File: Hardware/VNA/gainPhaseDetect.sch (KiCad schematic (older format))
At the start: 34 parts, among them U14 F2923, U15 AD8302

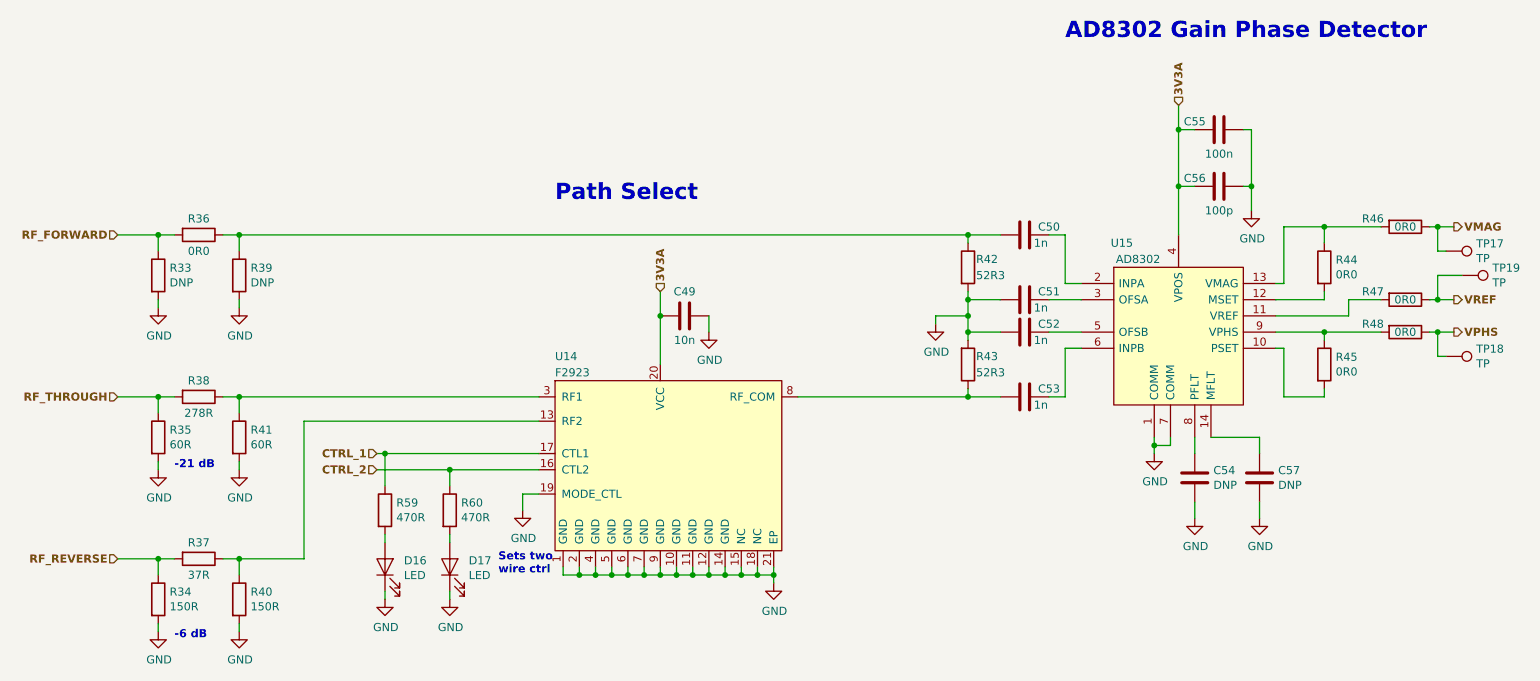
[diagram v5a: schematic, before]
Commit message: fix KiCad 5.1.0 bold after plot issue on schematics
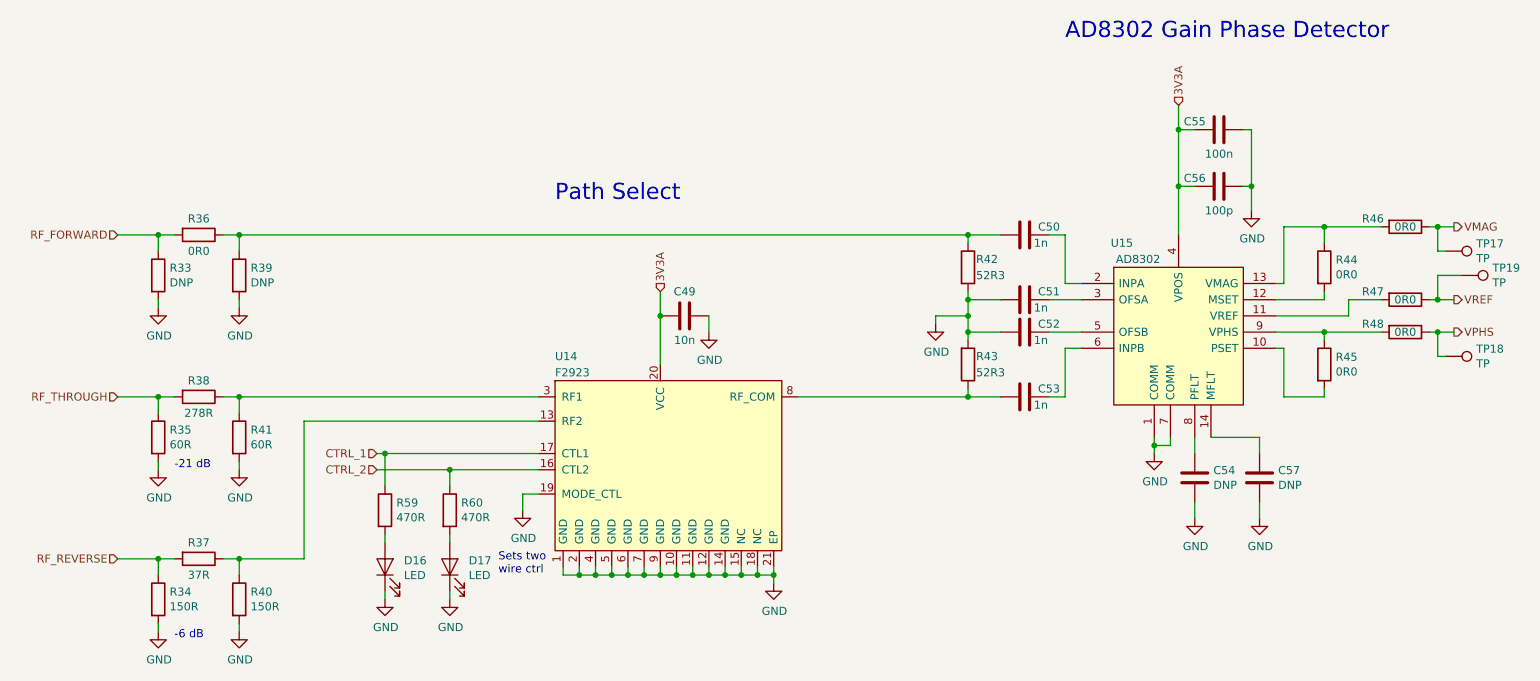
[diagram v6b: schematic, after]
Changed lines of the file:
@@
 Comment4 ""
 $EndDescr
-Text HLabel 1550 4000 0    50   Input ~ 10
+Text HLabel 1550 4000 0    50   Input ~ 0
 RF_THROUGH
 Wire Wire Line
@@
 	1800 5000 1550 5000
 Connection ~ 1800 5000
-Text HLabel 1550 5000 0    50   Input ~ 10
+Text HLabel 1550 5000 0    50   Input ~ 0
 RF_REVERSE
 Wire Wire Line
@@
 	1800 4000 1550 4000
 Connection ~ 1800 4000
-Text Notes 1900 4450 0    50   ~ 10
+Text Notes 1900 4450 0    50   ~ 0
 -21 dB
 Wire Wire Line
 	4150 4150 2700 4150
 Connection ~ 2300 4000
-Text HLabel 3150 4350 0    50   Input ~ 10
+Text HLabel 3150 4350 0    50   Input ~ 0
 CTRL_1
-Text HLabel 3150 4450 0    50   Input ~ 10
+Text HLabel 3150 4450 0    50   Input ~ 0
 CTRL_2
 Wire Wire Line
@@
 	5600 5150 5600 5100
 Connection ~ 5600 5100
-Text HLabel 1550 3000 0    50   Input ~ 10
+Text HLabel 1550 3000 0    50   Input ~ 0
 RF_FORWARD
 Wire Wire Line
@@
 	4900 3350 4900 3500
 Connection ~ 4900 3500
-Text HLabel 9800 2950 2    50   Output ~ 10
+Text HLabel 9800 2950 2    50   Output ~ 0
 VMAG
-Text HLabel 9800 3400 2    50   Output ~ 10
+Text HLabel 9800 3400 2    50   Output ~ 0
 VREF
-Text HLabel 9800 3600 2    50   Output ~ 10
+Text HLabel 9800 3600 2    50   Output ~ 0
 VPHS
-Text HLabel 4900 3350 1    50   Input ~ 10
+Text HLabel 4900 3350 1    50   Input ~ 0
 3V3A
 Wire Wire Line
@@
 Wire Wire Line
 	2300 3000 6800 3000
-Text HLabel 8100 2200 1    50   Input ~ 10
+Text HLabel 8100 2200 1    50   Input ~ 0
 3V3A
 Wire Wire Line
@@
 Wire Wire Line
 	8550 2700 8550 2850
-Text Notes 4250 2800 0    100  ~ 20
+Text Notes 4250 2800 0    100  ~ 0
 Path Select
-Text Notes 7400 1800 0    100  ~ 20
+Text Notes 7400 1800 0    100  ~ 0
 AD8302 Gain Phase Detector
-Text Notes 1900 5500 0    50   ~ 10
+Text Notes 1900 5500 0    50   ~ 0
 -6 dB
 $Comp
@@
 	5750 4000 6800 4000
 Connection ~ 2300 3000
-Text Notes 3900 5100 0    50   ~ 10
+Text Notes 3900 5100 0    50   ~ 0
 Sets two \nwire ctrl
 Wire Wire Line
